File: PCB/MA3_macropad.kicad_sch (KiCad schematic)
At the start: 65 parts, among them SW1 SW_Push, SW10 SW_Push, SW11 SW_Push, SW12 SW_Push, SW13 SW_Push, SW14 SW_Push, SW15 SW_Push, SW16 SW_Push, SW2 SW_Push, SW3 SW_Push, SW4 SW_Push, SW5 SW_Push, SW6 SW_Push, SW7 SW_Push, SW8 SW_Push, SW9 SW_Push, U1 XIAO-RP2040-SMD, U2 MCP23017x-x-SP, U3 ER_OLEDM0.91_1x-I2C

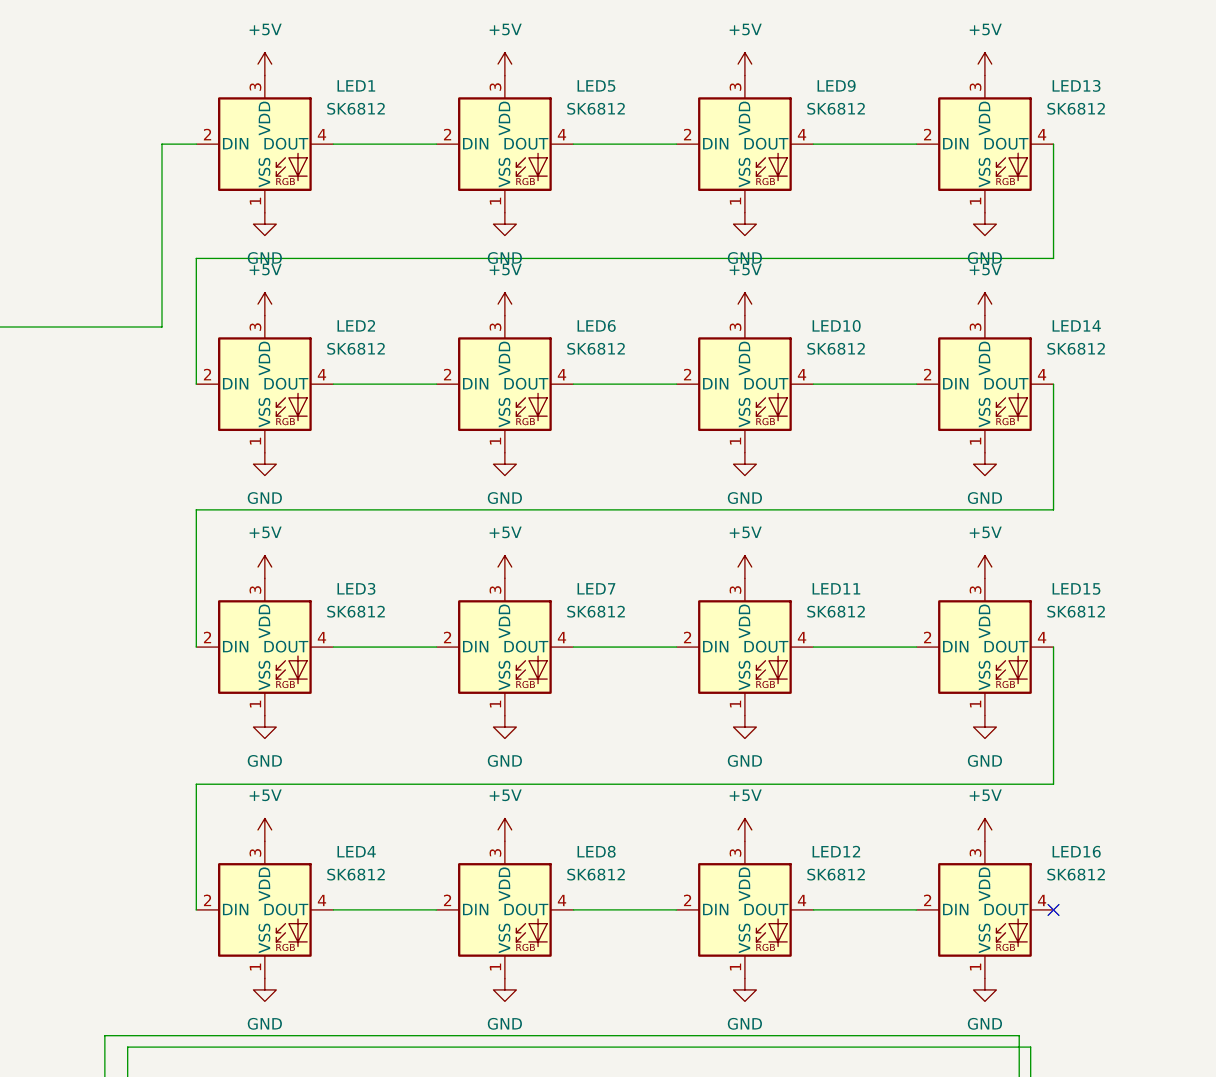
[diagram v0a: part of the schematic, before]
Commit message: Changed file storage
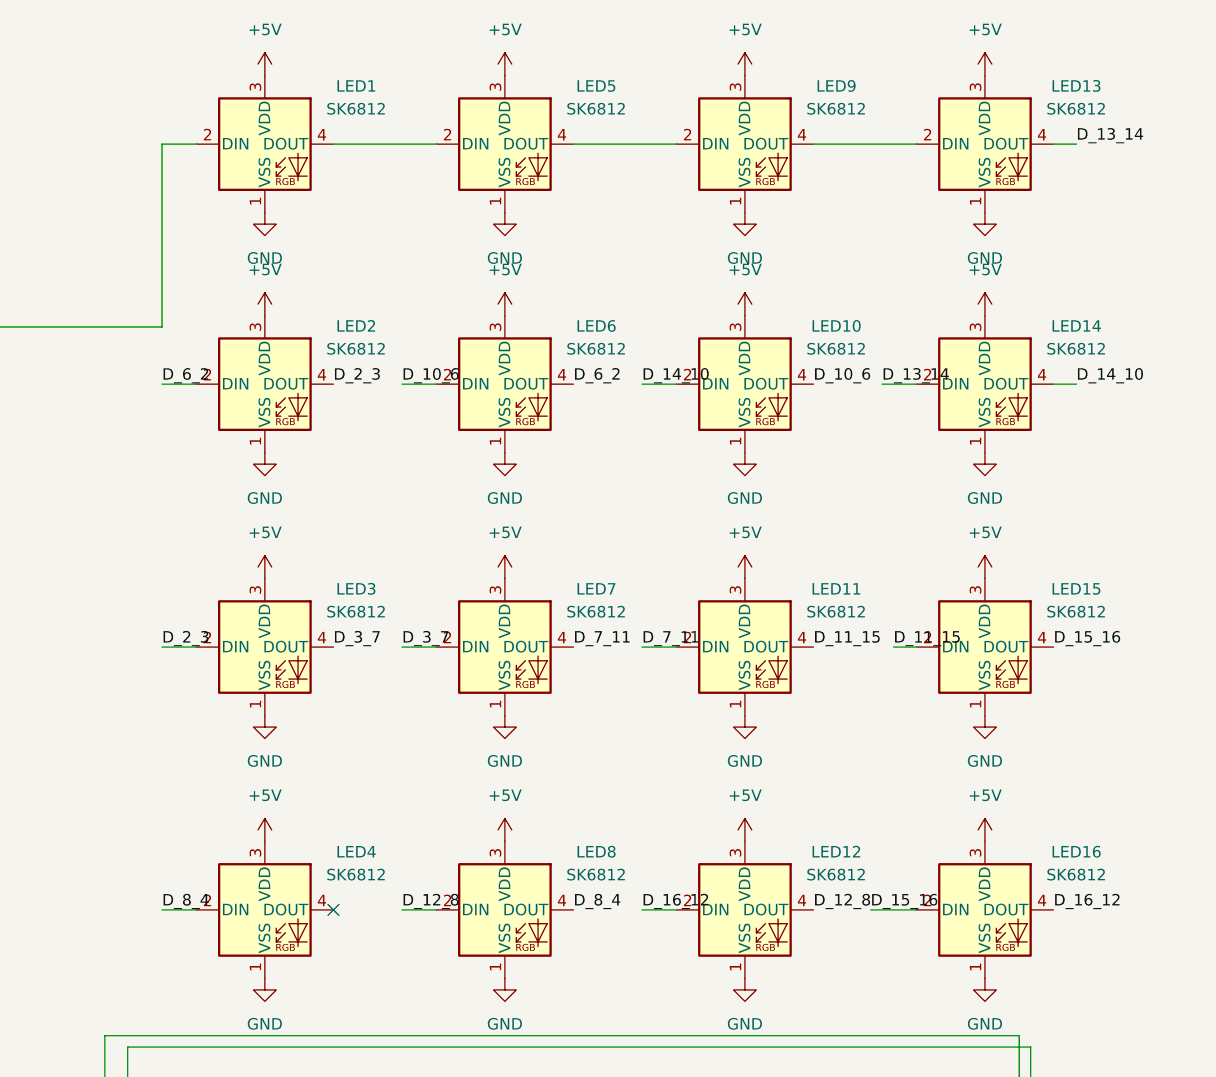
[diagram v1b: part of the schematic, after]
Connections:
- net D_3_7: now reaches LED3.4 (DOUT), LED7.2 (DIN)
- net D_7_11: now reaches LED11.2 (DIN), LED7.4 (DOUT)
- net D_13_14: now reaches LED13.4 (DOUT)
- net D_13_14: now also LED14.2 (DIN); no longer LED2.2 (DIN)
- net D_10_6: now reaches LED6.2 (DIN)
- net D_10_6: now also LED10.4 (DOUT); no longer LED2.4 (DOUT)
- net D_14_10: now reaches LED14.4 (DOUT)
- net D_14_10: now also LED10.2 (DIN); no longer LED3.2 (DIN)
- net D_11_15: now reaches LED11.4 (DOUT), LED15.2 (DIN)
- net D_15_16: now reaches LED15.4 (DOUT)
- net D_15_16: now also LED16.2 (DIN); no longer LED4.2 (DIN)
- net at LED4.4 (DOUT): no longer LED8.2 (DIN)
- net D_6_2: now reaches LED6.4 (DOUT)
- net D_6_2: now also LED2.2 (DIN); no longer LED10.2 (DIN)
- net D_16_12: now reaches LED12.2 (DIN)
- net D_16_12: now also LED16.4 (DOUT); no longer LED8.4 (DOUT)
- net D_12_8: now reaches LED12.4 (DOUT)
- net D_12_8: now also LED8.2 (DIN); no longer LED16.2 (DIN)
- new net D_2_3: LED2.4 (DOUT), LED3.2 (DIN)
- new net D_8_4: LED4.2 (DIN), LED8.4 (DOUT)
